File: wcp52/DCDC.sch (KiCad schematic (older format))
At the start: 52 parts, among them Q13 MMBT3904, Q15 MMBT3904, Q16 MMBT3904, Q17 PZT2907A, Q18 PZT2907A, Q19 MMBT3904, U14 L78M05CDT, U15 MC79M05CDT, U16 AZ1117CH-1.8TRG1, U17 MCP1700T-vv02E/TT

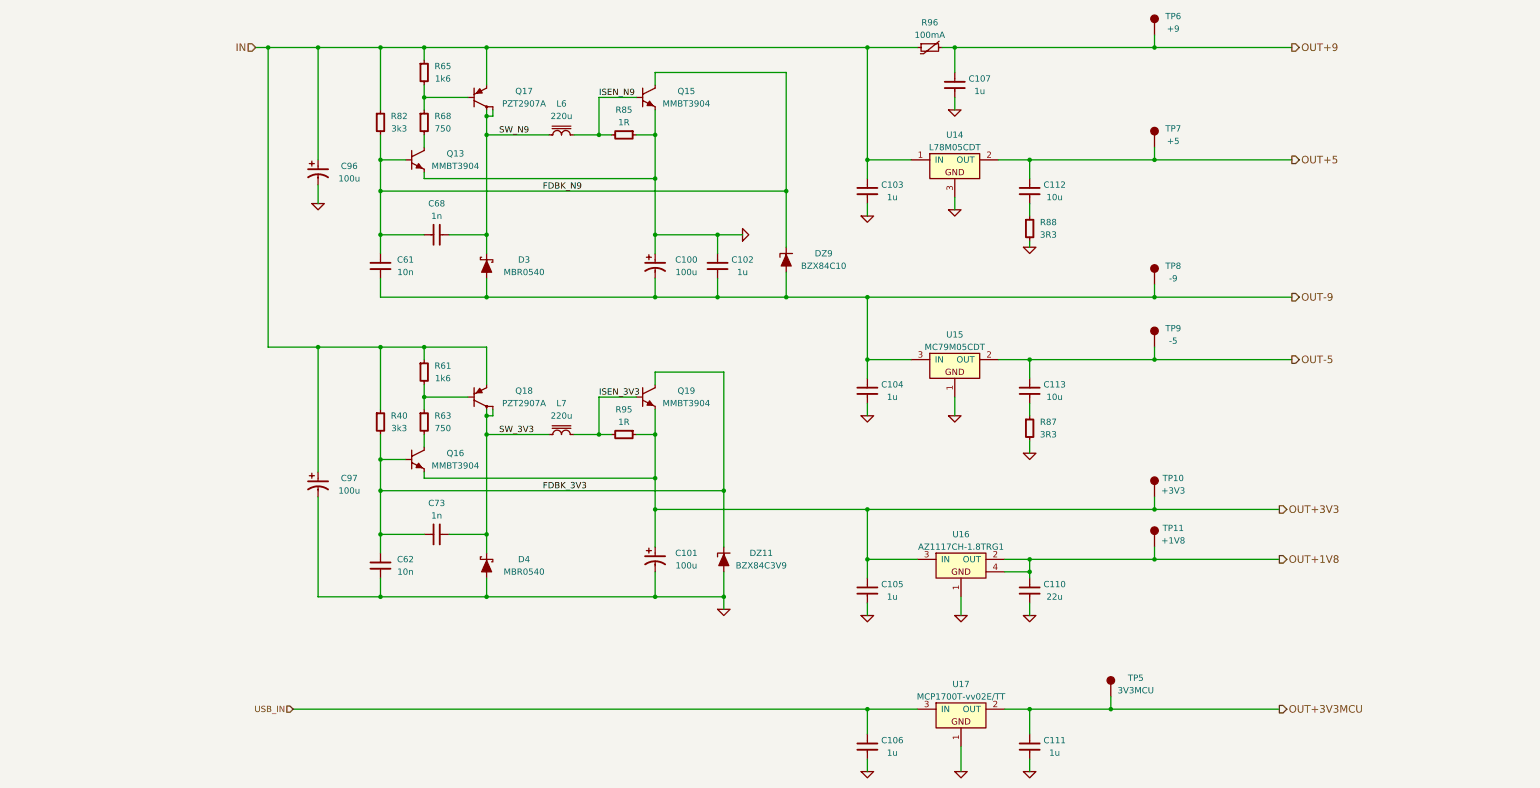
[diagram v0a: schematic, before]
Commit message: Add PSU filter inductors
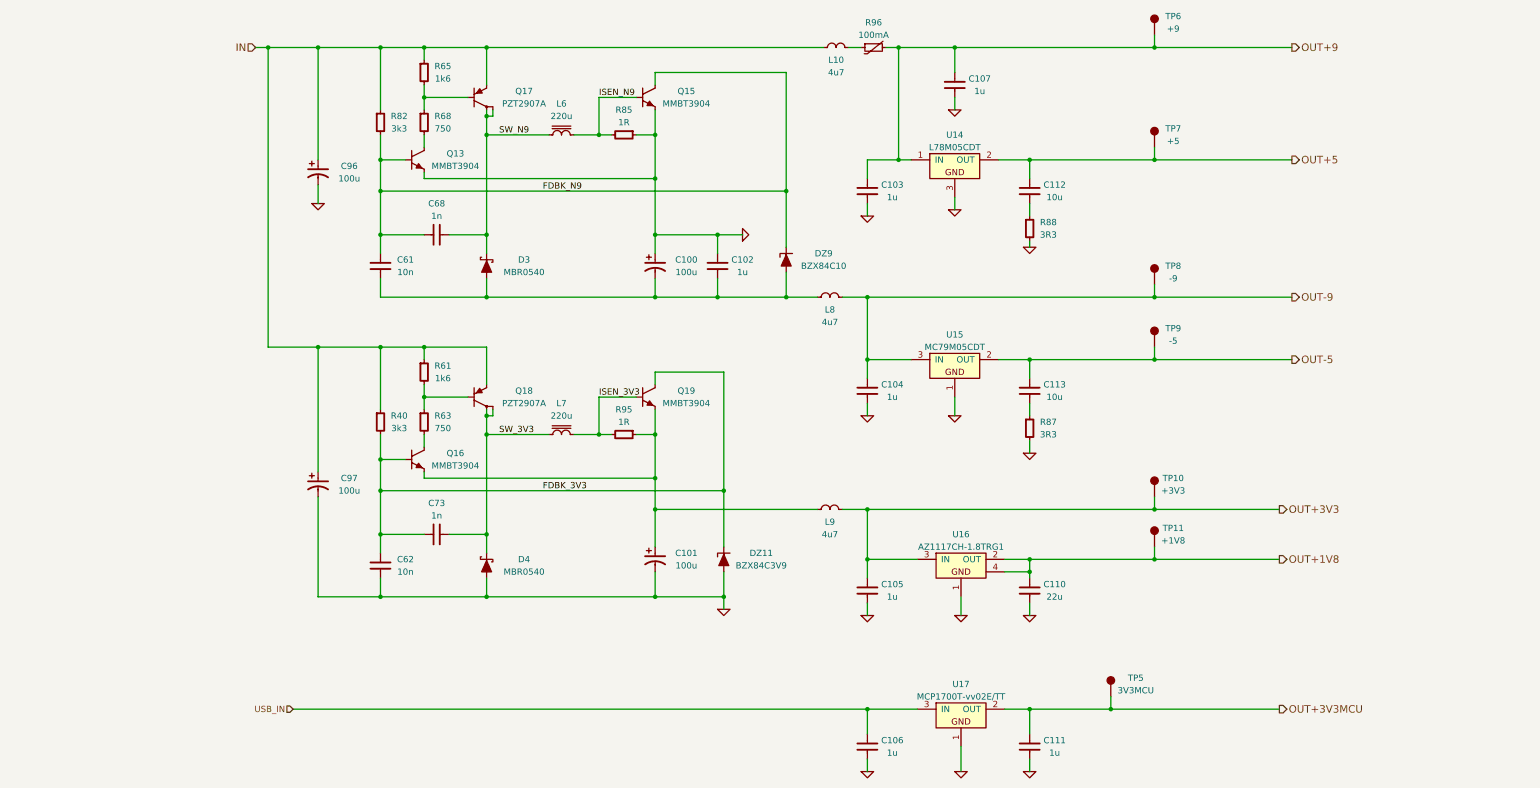
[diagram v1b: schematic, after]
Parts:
- added L10, L8, L9: 4u7, IPC7351-Nominal:INDC2012X130, symbol L-0805
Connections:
- net IN: now also L10.2; no longer C103.1, R96.1, U14.1 (IN)
- net OUT+3V3: now also L9.1; no longer C101.1, Q16.2, Q19.2, R95.1
- net OUT+9: now also C103.1, U14.1 (IN)
- net OUT-9: now also L8.1; no longer C100.2, C102.2, C61.2, D3.2, DZ9.1
- new net: C100.2, C102.2, C61.2, D3.2, DZ9.1, L8.2
- new net: C101.1, L9.2, Q16.2, Q19.2, R95.1
- new net: L10.1, R96.1
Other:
- moved on the sheet: R96
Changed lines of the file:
@@
 L THERM R96
 U 1 1 54F8BDC0
-P 8150 1000
-F 0 "R96" V 7950 1000 50  0000 C CNN
-F 1 "100mA" V 8050 1000 50  0000 C CNN
-F 2 "IPC7351-Nominal:RESC3216X60" H 8150 1050 60  0001 C CNN
-F 3 "" H 8150 1050 60  0000 C CNN
-F 4 "0ZCJ0010FF2E" H 8150 1000 60  0001 C CNN "PN"
-F 5 "BelFuse" H 8150 1000 60  0001 C CNN "Manuf"
-F 6 "DIST DIGIKEY 507-1794-1-ND" H 8150 1000 60  0001 C CNN "BOM"
-	1    8150 1000
+P 7700 1000
+F 0 "R96" V 7500 1000 50  0000 C CNN
+F 1 "100mA" V 7600 1000 50  0000 C CNN
+F 2 "IPC7351-Nominal:RESC3216X60" H 7700 1050 60  0001 C CNN
+F 3 "" H 7700 1050 60  0000 C CNN
+F 4 "0ZCJ0010FF2E" H 7700 1000 60  0001 C CNN "PN"
+F 5 "BelFuse" H 7700 1000 60  0001 C CNN "Manuf"
+F 6 "DIST DIGIKEY 507-1794-1-ND" H 7700 1000 60  0001 C CNN "BOM"
+	1    7700 1000
 	0    -1   1    0
 $EndComp
@@
 	3750 1000 3750 1500
 Wire Wire Line
-	2750 1000 8050 1000
-Wire Wire Line
 	4600 1000 4600 1300
 Wire Wire Line
@@
 Wire Wire Line
 	2850 3400 4600 3400
-Wire Wire Line
-	5950 4700 10950 4700
 Connection ~ 5950 4700
 Wire Wire Line
@@
 Connection ~ 4600 1000
 Wire Wire Line
-	8250 1000 11050 1000
+	7800 1000 11050 1000
 Wire Wire Line
 	8350 1000 8350 1200
@@
 Connection ~ 8350 1000
 Wire Wire Line
-	7650 1000 7650 2050
-Wire Wire Line
 	7650 1900 8000 1900
-Connection ~ 7650 1000
 Wire Wire Line
 	8350 2300 8350 2200
-Connection ~ 7650 1900
 Wire Wire Line
 	7650 2350 7650 2250
@@
 Wire Wire Line
 	3250 2250 3250 2100
-Wire Wire Line
-	3750 3000 11050 3000
 Wire Wire Line
 	9600 6200 9600 6300
@@
 $EndComp
 Wire Wire Line
-	9950 2900 9950 3000
+	9950 3000 9950 2900
 Connection ~ 9950 3000
 $Comp
@@
 $EndComp
 Wire Wire Line
-	9950 4600 9950 4700
+	9950 4700 9950 4600
 Connection ~ 9950 4700
 $Comp
@@
 	1    0    0    -1
 $EndComp
+$Comp
+L L-0805 L8
+U 1 1 5503A3B0
+P 7350 3000
+F 0 "L8" V 7450 3000 50  0000 C CNN
+F 1 "4u7" V 7550 3000 50  0000 C CNN
+F 2 "IPC7351-Nominal:INDC2012X130" H 7350 3000 50  0001 C CNN
+F 3 "" H 7350 3050 60  0000 C CNN
+F 4 "MLZ2012M4R7HT000" H 7350 3000 60  0001 C CNN "PN"
+F 5 "TDK" H 7350 3000 60  0001 C CNN "Manuf"
+F 6 "DIST DIGIKEY 445-8659-1-ND" H 7350 3000 60  0001 C CNN "BOM"
+	1    7350 3000
+	0    1    1    0
+$EndComp
+Wire Wire Line
+	7450 3000 11050 3000
+Wire Wire Line
+	3750 3000 7250 3000
+$Comp
+L L-0805 L9
+U 1 1 5503B1A4
+P 7350 4700
+F 0 "L9" V 7450 4700 50  0000 C CNN
+F 1 "4u7" V 7550 4700 50  0000 C CNN
+F 2 "IPC7351-Nominal:INDC2012X130" H 7350 4700 50  0001 C CNN
+F 3 "" H 7350 4750 60  0000 C CNN
+F 4 "MLZ2012M4R7HT000" H 7350 4700 60  0001 C CNN "PN"
+F 5 "TDK" H 7350 4700 60  0001 C CNN "Manuf"
+F 6 "DIST DIGIKEY 445-8659-1-ND" H 7350 4700 60  0001 C CNN "BOM"
+	1    7350 4700
+	0    1    1    0
+$EndComp
+Wire Wire Line
+	7450 4700 10950 4700
+Wire Wire Line
+	7250 4700 5950 4700
+$Comp
+L L-0805 L10
+U 1 1 5503CCD9
+P 7400 1000
+F 0 "L10" V 7500 1000 50  0000 C CNN
+F 1 "4u7" V 7600 1000 50  0000 C CNN
+F 2 "IPC7351-Nominal:INDC2012X130" H 7400 1000 50  0001 C CNN
+F 3 "" H 7400 1050 60  0000 C CNN
+F 4 "MLZ2012M4R7HT000" H 7400 1000 60  0001 C CNN "PN"
+F 5 "TDK" H 7400 1000 60  0001 C CNN "Manuf"
+F 6 "DIST DIGIKEY 445-8659-1-ND" H 7400 1000 60  0001 C CNN "BOM"
+	1    7400 1000
+	0    1    1    0
+$EndComp
+Wire Wire Line
+	7500 1000 7600 1000
+Wire Wire Line
+	2750 1000 7300 1000
+Wire Wire Line
+	7900 1000 7900 1900
+Connection ~ 7900 1900
+Connection ~ 7900 1000
+Wire Wire Line
+	7650 1900 7650 2050
 $EndSCHEMATC

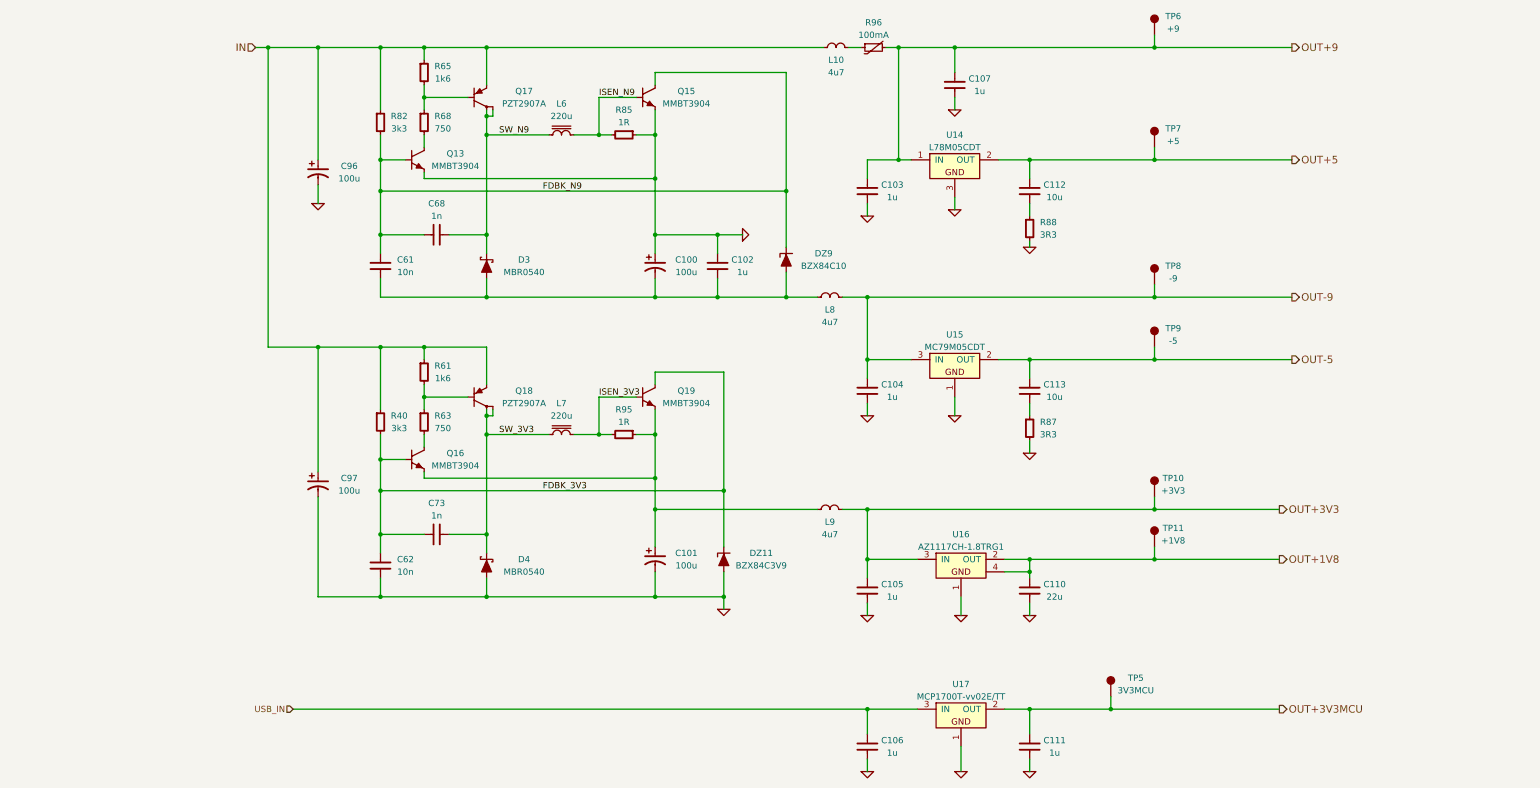
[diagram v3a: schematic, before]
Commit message: Reannotate parts. May need to tweak silkscreen
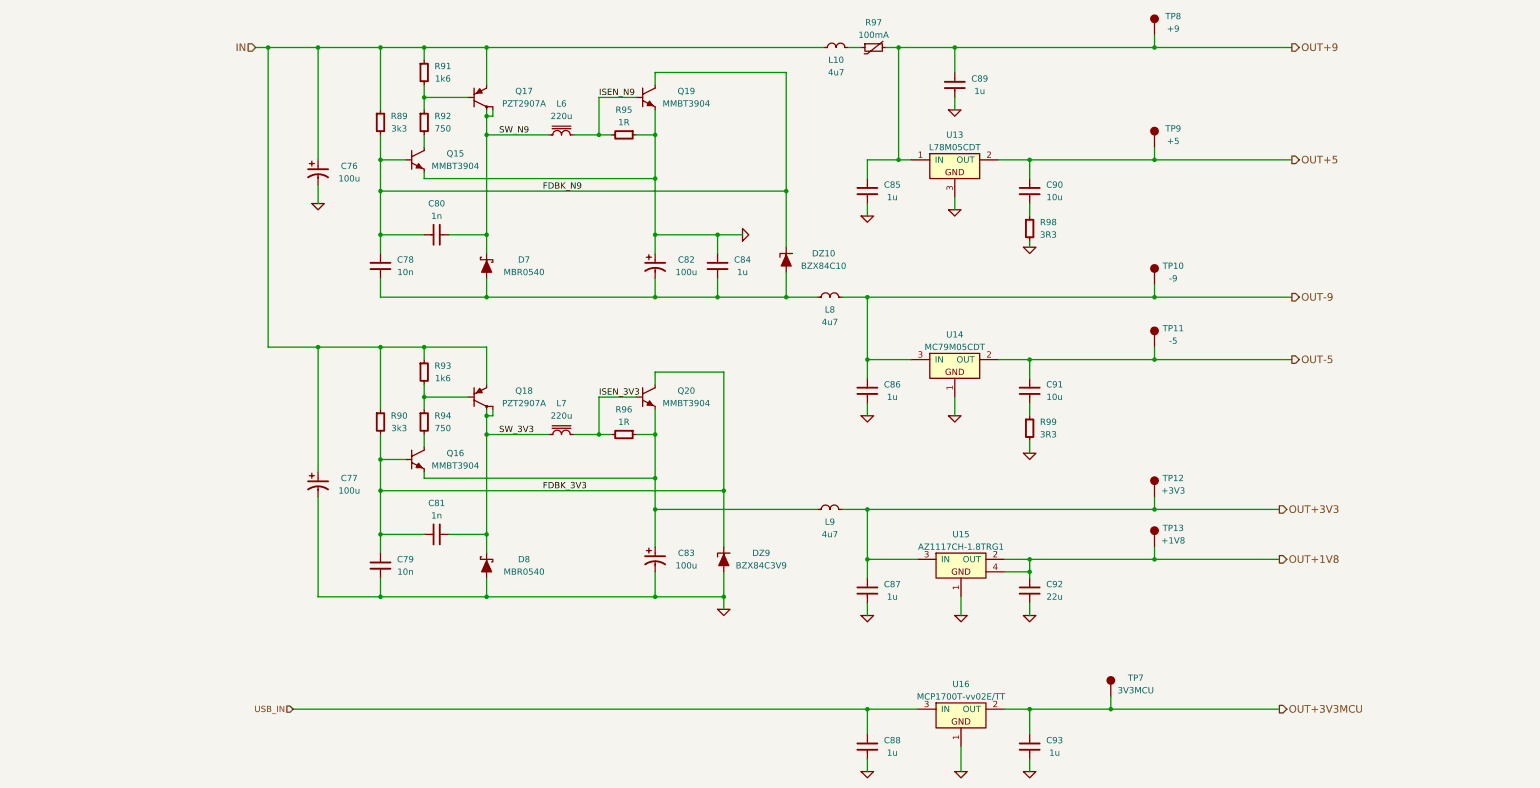
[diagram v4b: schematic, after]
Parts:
- C76: renamed from C96; OldReference (none) -> C96
- C77: renamed from C97; OldReference (none) -> C97
- C78: renamed from C61; OldReference (none) -> C61
- C79: renamed from C62; OldReference (none) -> C62
- C80: renamed from C68; OldReference (none) -> C68
- C81: renamed from C73; OldReference (none) -> C73
- C82: renamed from C100; OldReference (none) -> C100
- C83: renamed from C101; OldReference (none) -> C101
- C84: renamed from C102; OldReference (none) -> C102
- C85: renamed from C103; OldReference (none) -> C103
- C86: renamed from C104; OldReference (none) -> C104
- C87: renamed from C105; OldReference (none) -> C105
- C88: renamed from C106; OldReference (none) -> C106
- C89: renamed from C107; OldReference (none) -> C107
- C90: renamed from C112; OldReference (none) -> C112
- C91: renamed from C113; OldReference (none) -> C113
- C92: renamed from C110; OldReference (none) -> C110
- C93: renamed from C111; OldReference (none) -> C111
- D7: renamed from D3; OldReference (none) -> D3
- D8: renamed from D4; OldReference (none) -> D4
- DZ10: renamed from DZ9; OldReference (none) -> DZ9
- DZ9: renamed from DZ11; OldReference (none) -> DZ11
- L10: OldReference (none) -> L10
- L6: OldReference (none) -> L6
- L7: OldReference (none) -> L7
- L8: OldReference (none) -> L8
- L9: OldReference (none) -> L9
- Q15: renamed from Q13; OldReference (none) -> Q13
- Q16: OldReference (none) -> Q16
- Q17: OldReference (none) -> Q17
- Q18: OldReference (none) -> Q18
- Q19: renamed from Q15; OldReference (none) -> Q15
- Q20: renamed from Q19; OldReference (none) -> Q19
- R89: renamed from R82; OldReference (none) -> R82
- R90: renamed from R40; OldReference (none) -> R40
- R91: renamed from R65; OldReference (none) -> R65
- R92: renamed from R68; OldReference (none) -> R68
- R93: renamed from R61; OldReference (none) -> R61
- R94: renamed from R63; OldReference (none) -> R63
- R95: renamed from R85; OldReference (none) -> R85
- R96: renamed from R95; OldReference (none) -> R95
- R97: renamed from R96; OldReference (none) -> R96
- R98: renamed from R88; OldReference (none) -> R88
- R99: renamed from R87; OldReference (none) -> R87
- TP10: renamed from TP8; OldReference (none) -> TP8
- TP11: renamed from TP9; OldReference (none) -> TP9
- TP12: renamed from TP10; OldReference (none) -> TP10
- TP13: renamed from TP11; OldReference (none) -> TP11
- TP7: renamed from TP5; OldReference (none) -> TP5
- TP8: renamed from TP6; OldReference (none) -> TP6
- TP9: renamed from TP7; OldReference (none) -> TP7
- U13: renamed from U14; OldReference (none) -> U14
- U14: renamed from U15; OldReference (none) -> U15
- U15: renamed from U16; OldReference (none) -> U16
- U16: renamed from U17; OldReference (none) -> U17

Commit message: Schematic touchups
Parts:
- U16: value MCP1700T-vv02E/TT -> MCP1700T-3302E/TT; BOM (none) -> DIST DIGIKEY MCP1700T3302ETTCT-ND
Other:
- note added: "The operation of this circuit is the same as for the buck converter,\nbelow. Note a useful characteristic of the buck converter: by\nswapping the positions of the outputs (connecting the positive\noutput to ground, and using what was ground as the negative output),\nthe circuit can be repurposed as a "buck-boost" (inverting) converter."
- note added: "This circuit is a buck converter, which converts the 9V input into\nan approximatly 3.3V output.\n\n- Whenever @Q16 switches on, it draws @Q18's base negative, switching on\n @Q18 as well.\n- When @Q16's base is less than 0.65V above its emitter (like at startup), it will\n charge as current flows through @R90 into @C79.\n- Once the base voltage is 0.65V above the emitter, @Q16 starts to turn on,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"
- moved on the sheet: C76, C77, C78, C79, C80, C81, C82, C83, C84, C85, C86, C87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
